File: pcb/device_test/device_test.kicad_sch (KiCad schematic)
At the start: 13 parts, among them J101 Screw_Terminal_01x02, J102 Conn_01x05, J103 Conn_01x05, J104 USB_OTG, J105 USB_A, J106 Conn_01x07, J107 Conn_01x06

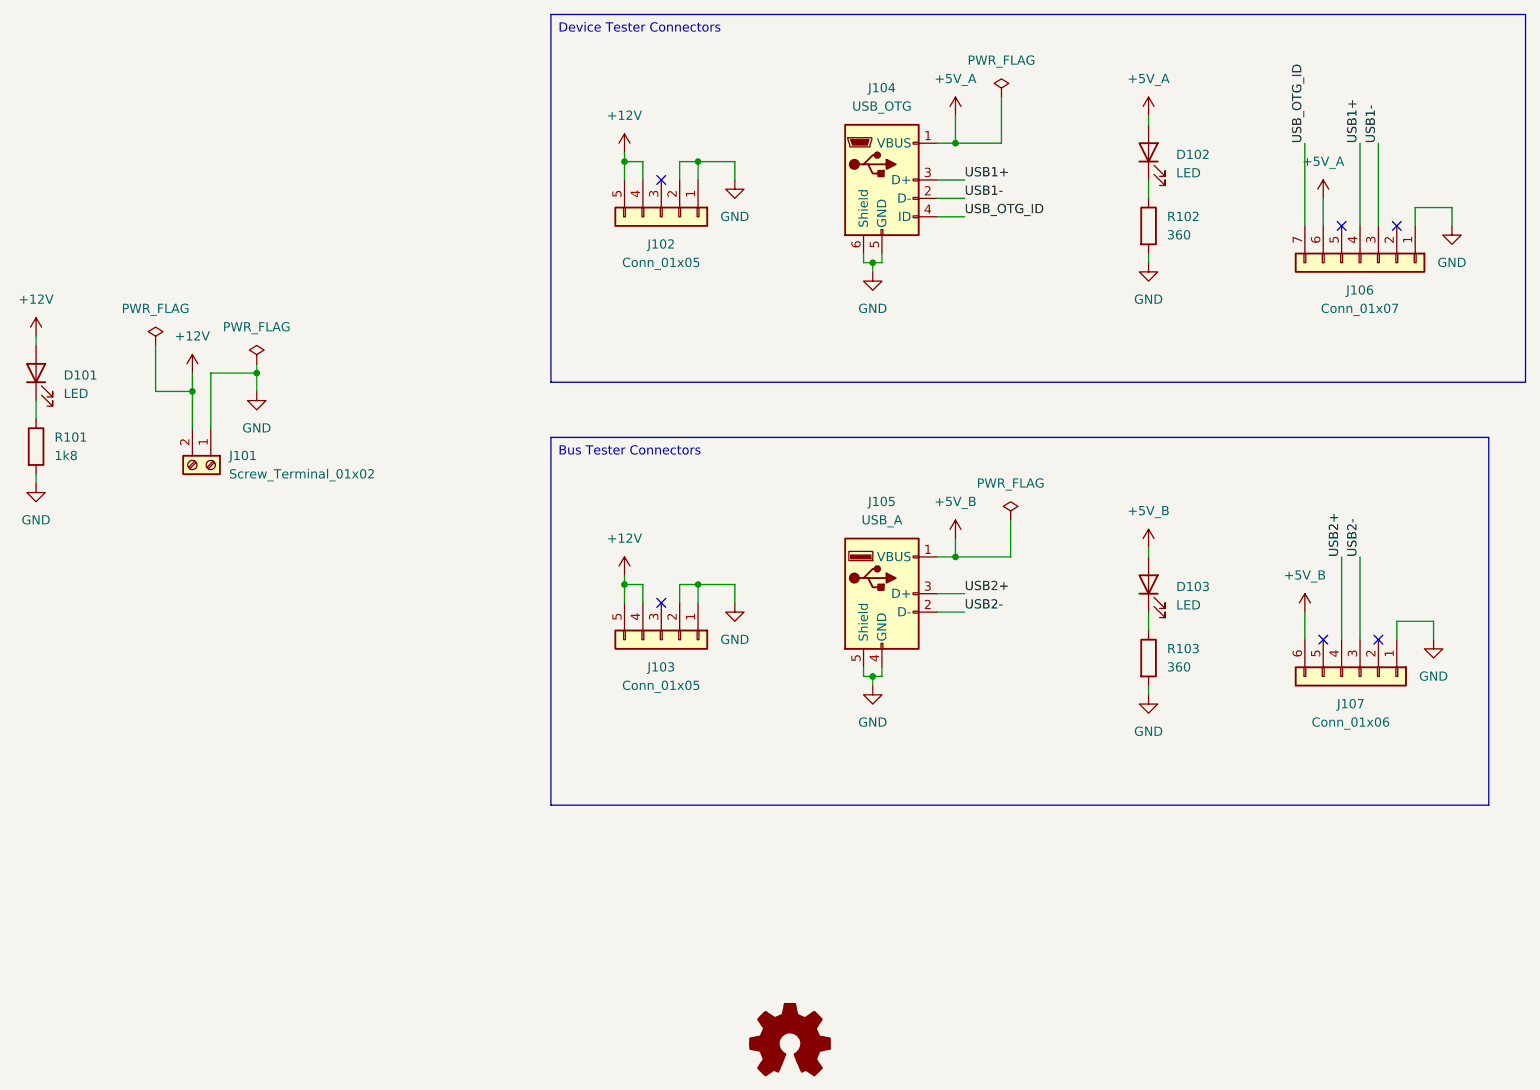
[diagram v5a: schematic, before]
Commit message: update connectors
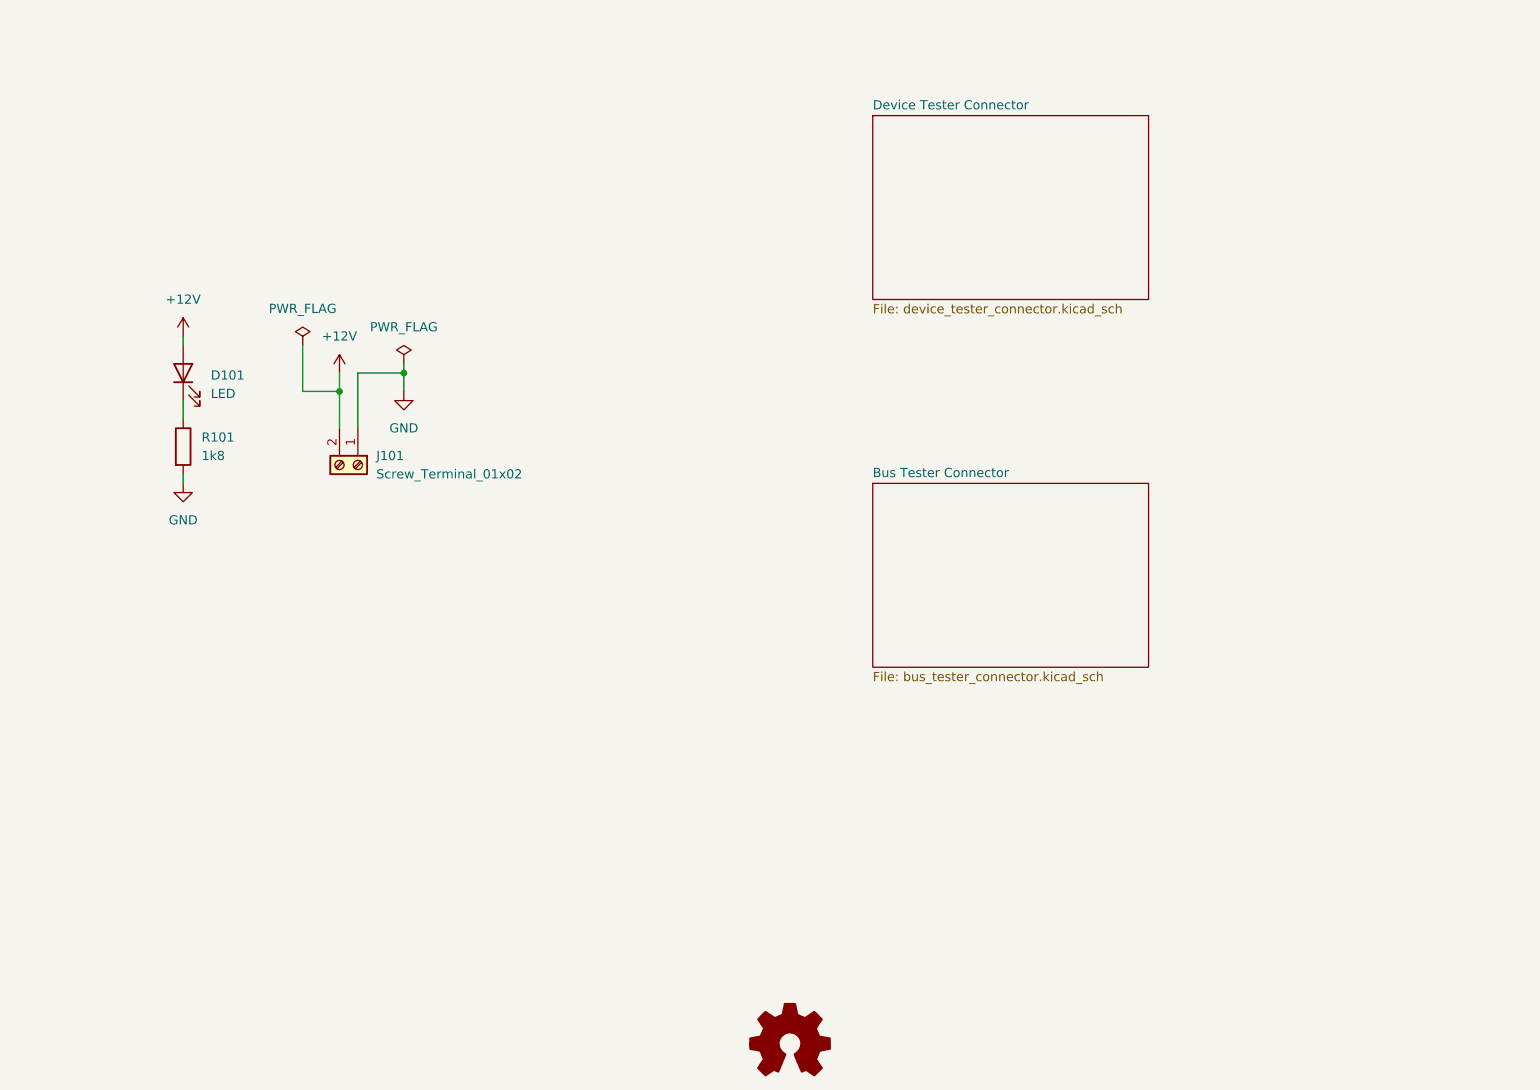
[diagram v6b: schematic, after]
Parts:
- removed D102, D103: LED, LED_SMD:LED_0805_2012Metric, symbol Device:LED
- removed J102: Conn_01x05, Connector_PinSocket_2.54mm:PinSocket_1x05_P2.54mm_Horizontal, symbol Connector_Generic:Conn_01x05
- removed J103: Conn_01x05, Connector_PinHeader_2.54mm:PinHeader_1x05_P2.54mm_Horizontal, symbol Connector_Generic:Conn_01x05
- removed J104: USB_OTG, USB:MicroUSB-920-E52A2021S10100, symbol Connector:USB_OTG
- removed J105: USB_A, USB:USB_A_C456020, symbol Connector:USB_A
- removed J106: Conn_01x07, Connector_PinSocket_2.54mm:PinSocket_1x07_P2.54mm_Horizontal, symbol Connector_Generic:Conn_01x07
- removed J107: Conn_01x06, Connector_PinHeader_2.54mm:PinHeader_1x06_P2.54mm_Horizontal, symbol Connector_Generic:Conn_01x06
- removed R102, R103: 360, Resistor_SMD:R_0805_2012Metric, symbol Device:R
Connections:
- no-connect marks 6 -> 0
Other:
- added sheet Bus Tester Connector (bus_tester_connector.kicad_sch)
- added sheet Device Tester Connector (device_tester_connector.kicad_sch)
- title: Device Tester Connectors -> Device Tester
- moved on the sheet: D101, J101, R101

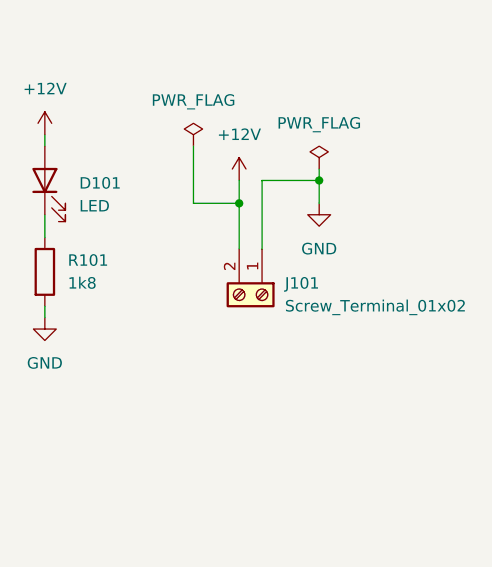
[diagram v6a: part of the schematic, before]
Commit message: update LCSC codes
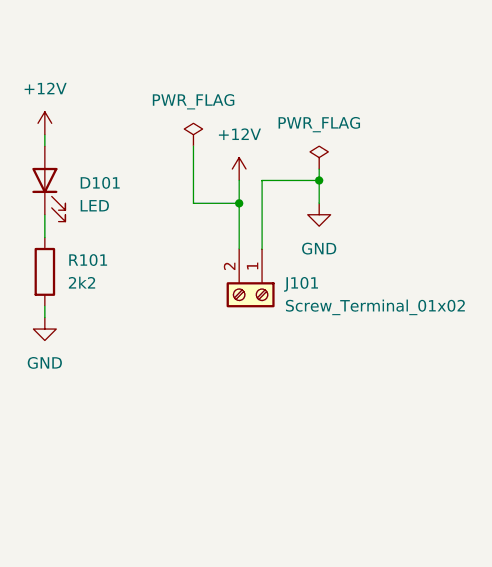
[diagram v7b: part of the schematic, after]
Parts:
- D101: LCSC (none) -> C84256
- J101: footprint TerminalBlock_Phoenix:TerminalBlock_Phoenix_MKDS-1,5-2_1x02_P5.00mm_Horizontal -> TerminalBlock_Phoenix:TerminalBlock_Phoenix_MKDS-1,5-2-5.08_1x02_P5.08mm_Horizontal; LCSC (none) -> C5349557
- R101: value 1k8 -> 2k2; LCSC (none) -> C17520
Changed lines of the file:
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@@
 			)
 		)
-		(property "Footprint" "TerminalBlock_Phoenix:TerminalBlock_Phoenix_MKDS-1,5-2_1x02_P5.00mm_Horizontal"
+		(property "Footprint" "TerminalBlock_Phoenix:TerminalBlock_Phoenix_MKDS-1,5-2-5.08_1x02_P5.08mm_Horizontal"
 			(at 93.98 99.06 0)
 			(effects
@@
 			)
 		)
-		(property "LCSC" ""
+		(property "LCSC" "C5349557"
 			(at 93.98 99.06 0)
 			(effects
@@
 			)
 		)
-		(property "LCSC" ""
+		(property "LCSC" "C84256"
 			(at 69.85 86.36 0)
 			(effects
@@
 			)
 		)
-		(property "Value" "1k8"
+		(property "Value" "2k2"
 			(at 72.39 97.7899 0)
 			(effects
@@
 			)
 		)
-		(property "LCSC" ""
+		(property "LCSC" "C17520"
 			(at 69.85 96.52 0)
 			(effects

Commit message: add caps
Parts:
- added C101: 100u / 25V, Capacitor_Tantalum_SMD:CP_EIA-7343-43_Kemet-X_Pad2.25x2.55mm_HandSolder, symbol Device:C_Polarized
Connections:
- net +12V: now also C101.1
- net GND: now also C101.2
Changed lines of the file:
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@@
+	(wire
+		(pts
+			(xy 130.81 91.44) (xy 130.81 93.98)
+		)
+		(stroke
+			(width 0)
+			(type default)
+		)
+	)
 	(wire
 		(pts
@@
 	(wire
 		(pts
-			(xy 93.98 93.98) (xy 93.98 86.36)
+			(xy 130.81 81.28) (xy 130.81 83.82)
 		)
 		(stroke
@@
 		)
 	)
+	(wire
+		(pts
+			(xy 93.98 93.98) (xy 93.98 86.36)
+		)
+		(stroke
+			(width 0)
+			(type default)
+		)
+	)
 	(symbol
 		(lib_id "power:GND")
@@
 	)
 	(symbol
+		(lib_id "Device:C_Polarized")
+		(at 130.81 87.63 0)
+		(unit 1)
+		(exclude_from_sim no)
+		(in_bom yes)
+		(on_board yes)
+		(dnp no)
+		(fields_autoplaced yes)
+		(property "Reference" "C101"
+			(at 134.62 85.4709 0)
+			(effects
+				(font
+					(size 1.27 1.27)
+				)
+				(justify left)
+			)
+		)
+		(property "Value" "100u / 25V"
+			(at 134.62 88.0109 0)
+			(effects
+				(font
+					(size 1.27 1.27)
+				)
+				(justify left)
+			)
+		)
+		(property "Footprint" "Capacitor_Tantalum_SMD:CP_EIA-7343-43_Kemet-X_Pad2.25x2.55mm_HandSolder"
+			(at 131.7752 91.44 0)
+			(effects
+				(font
+					(size 1.27 1.27)
+				)
+				(hide yes)
+			)
+		)
+		(property "Datasheet" "~"
+			(at 130.81 87.63 0)
+			(effects
+				(font
+					(size 1.27 1.27)
+				)
+				(hide yes)
+			)
+		)
+		(property "Description" "Polarized capacitor"
+			(at 130.81 87.63 0)
+			(effects
+				(font
+					(size 1.27 1.27)
+				)
+				(hide yes)
+			)
+		)
+		(property "LCSC" "C7230"
+			(at 130.81 87.63 0)
+			(effects
+				(font
+					(size 1.27 1.27)
+				)
+				(hide yes)
+			)
+		)
+		(pin "2"
+		)
+		(pin "1"
+		)
+		(instances
+			(project ""
+				(path "/5d20b266-567e-45c6-9e3e-145c2aea1daa"
+					(reference "C101")
+					(unit 1)
+				)
+			)
+		)
+	)
+	(symbol
 		(lib_id "power:PWR_FLAG")
 		(at 100.33 85.09 0)
@@
 	)
 	(symbol
+		(lib_id "power:+12V")
+		(at 130.81 81.28 0)
+		(unit 1)
+		(exclude_from_sim no)
+		(in_bom yes)
+		(on_board yes)
+		(dnp no)
+		(fields_autoplaced yes)
+		(property "Reference" "#PWR0106"
+			(at 130.81 85.09 0)
+			(effects
+				(font
+					(size 1.27 1.27)
+				)
+				(hide yes)
+			)
+		)
+		(property "Value" "+12V"
+			(at 130.81 76.2 0)
+			(effects
+				(font
+					(size 1.27 1.27)
+				)
+			)
+		)
+		(property "Footprint" ""
+			(at 130.81 81.28 0)
+			(effects
+				(font
+					(size 1.27 1.27)
+				)
+				(hide yes)
+			)
+		)
+		(property "Datasheet" ""
+			(at 130.81 81.28 0)
+			(effects
+				(font
+					(size 1.27 1.27)
+				)
+				(hide yes)
+			)
+		)
+		(property "Description" "Power symbol creates a global label with name \"+12V\""
+			(at 130.81 81.28 0)
+			(effects
+				(font
+					(size 1.27 1.27)
+				)
+				(hide yes)
+			)
+		)
+		(pin "1"
+		)
+		(instances
+			(project "device_test"
+				(path "/5d20b266-567e-45c6-9e3e-145c2aea1daa"
+					(reference "#PWR0106")
+					(unit 1)
+				)
+			)
+		)
+	)
+	(symbol
 		(lib_id "Device:R")
 		(at 69.85 96.52 0)
@@
 					(unit 1)
 				)
+			)
+		)
+	)
+	(symbol
+		(lib_id "power:GND")
+		(at 130.81 93.98 0)
+		(unit 1)
+		(exclude_from_sim no)
+		(in_bom yes)
+		(on_board yes)
+		(dnp no)
+		(fields_autoplaced yes)
+		(property "Reference" "#PWR0105"
+			(at 130.81 100.33 0)
+			(effects
+				(font
+					(size 1.27 1.27)
+				)
+				(hide yes)
+			)
+		)
+		(property "Value" "GND"
+			(at 130.81 99.06 0)
+			(effects
+				(font
+					(size 1.27 1.27)
+				)
+			)
+		)
+		(property "Footprint" ""
+			(at 130.81 93.98 0)
+			(effects
+				(font
+					(size 1.27 1.27)
+				)
+				(hide yes)
+			)
+		)
+		(property "Datasheet" ""
+			(at 130.81 93.98 0)
+			(effects
+				(font
+					(size 1.27 1.27)
+				)
+				(hide yes)
+			)
+		)
+		(property "Description" "Power symbol creates a global label with name \"GND\" , ground"
+			(at 130.81 93.98 0)
+			(effects
+				(font
+					(size 1.27 1.27)
+				)
+				(hide yes)
+			)
+		)
+		(pin "1"
+		)
+		(instances
+			(project "device_test"
+				(path "/5d20b266-567e-45c6-9e3e-145c2aea1daa"
+					(reference "#PWR0105")
+					(unit 1)
+				)
